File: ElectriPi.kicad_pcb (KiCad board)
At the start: 2 copper layers, 65 x 56 mm, 58 parts, among them IC2 TPS51397ARJER, J1 2444, J2 JST XH 01x02, J3 JST XH 01x02, J6 Raspberry_Pi_2_3, J8 JST XH 01x02, Q1 SiA471DJ, Q2 SiA430DJT, U1 LM74700, U2 COOLING

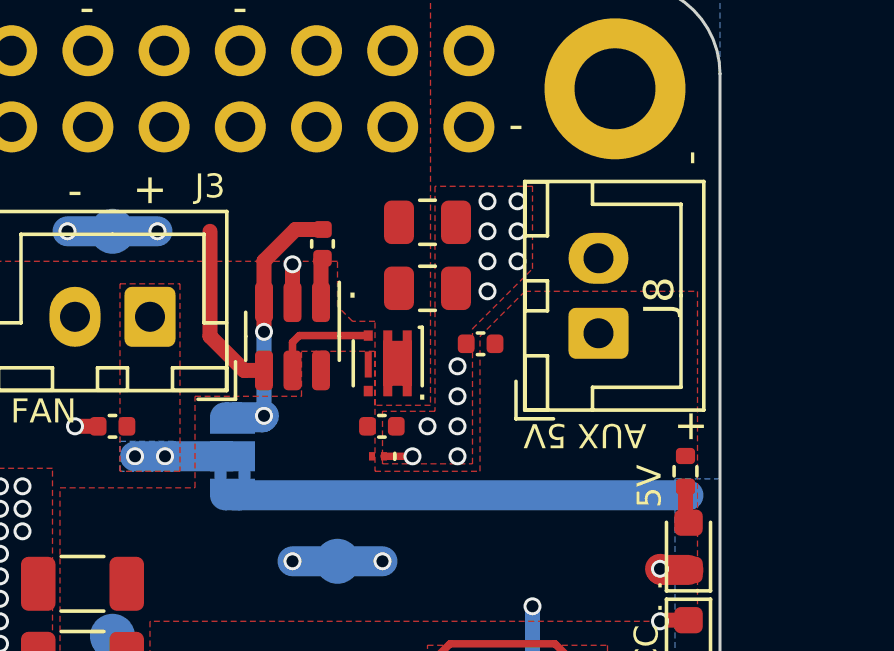
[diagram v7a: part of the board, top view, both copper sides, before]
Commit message: update holdup capacitance
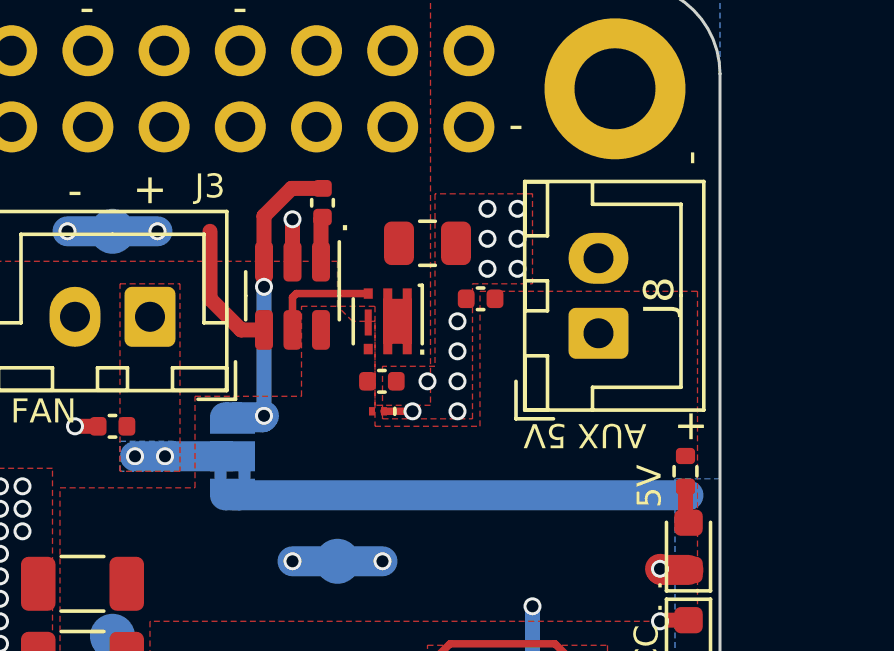
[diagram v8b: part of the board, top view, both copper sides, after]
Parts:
- removed C16: 22 uF, Capacitor_SMD:C_0805_2012Metric
- C11: value 22 uF -> 47uF
- moved C10 1.50 mm to (139.0, 66.5)
- moved C11 1.50 mm to (140.5, 61.9)
- moved C15 1.50 mm to (142.3, 63.8)
- moved D6 1.50 mm to (138.8, 67.5)
- moved Q2 1.40 mm to (139.2, 64.5)
- moved C9 1.37 mm to (137.0, 60.5)
- moved U1 1.35 mm to (136.0, 63.6)
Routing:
- net +5V: track 15.1 -> 16.6 mm
- net 5V_PI: track 8.77 -> 7.48 mm
- net GND: track 14.0 -> 14.2 mm, vias 109 -> 108
